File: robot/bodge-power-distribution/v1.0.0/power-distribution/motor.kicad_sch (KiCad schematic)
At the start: 6 parts, among them J4 MOTOR_{FL}, J5 MOTOR_{BL}, J6 MOTOR_{DRB}, J7 MOTOR_{AUX}, J8 MOTOR_{FR}, J9 MOTOR_{BR}

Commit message: Alpha (0.0.0)
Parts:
- added C30, C31: 10uF 63V, Capacitor_SMD:C_1210_3225Metric, symbol Device:C_Small
- added J12: MOTOR_{DRB}, AT-Connectors:1x02_P3mm_3x5mm_Plug_SMD, symbol Connector_Generic:Conn_01x02
- added J13: MOTOR_{AUX}, AT-Connectors:1x02_P3mm_3x5mm_Plug_SMD, symbol Connector_Generic:Conn_01x02
- added J16, J18: MOTOR_{FR}, AT-Connectors:1x02_P3mm_3x5mm_Plug_SMD, symbol Connector_Generic:Conn_01x02
- added J17: MOTOR_{BR}, AT-Connectors:1x02_P3mm_3x5mm_Plug_SMD, symbol Connector_Generic:Conn_01x02
- added J19: SERVO, Connector_PinSocket_2.54mm:PinSocket_1x03_P2.54mm_Vertical, symbol Connector_Generic:Conn_01x03
- added J8: MOTOR_{FL}, AT-Connectors:1x02_P3mm_3x5mm_Plug_SMD, symbol Connector_Generic:Conn_01x02
- added J9: MOTOR_{BL}, AT-Connectors:1x02_P3mm_3x5mm_Plug_SMD, symbol Connector_Generic:Conn_01x02
- added U7: DRV8220, Package_TO_SOT_SMD:SOT-563, symbol AT-PowerIC:DRV8220
- renumbered J6 to J10, J7 to J11, J8 to J14, J9 to J15, J4 to J6, J5 to J7
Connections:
- new net: J18.2 (Pin_2), U7.4 (OUT2)
- new net: J18.1 (Pin_1), U7.6 (OUT1)
- new net +12V: C30.1, U7.5 (VM)
- new net +5V: C31.1, J19.2 (Pin_2)
- new net +V_{BATT(PROTECTED)}: J12.1 (Pin_1), J13.1 (Pin_1), J16.1 (Pin_1), J17.1 (Pin_1), J8.1 (Pin_1), J9.1 (Pin_1)
- new net GND: C30.2, C31.2, J12.2 (Pin_2), J13.2 (Pin_2), J16.2 (Pin_2), J17.2 (Pin_2), J19.3 (Pin_3), J8.2 (Pin_2), J9.2 (Pin_2), U7.3 (GND)
- new net MOTOR_{BRUSHED}.IN1: U7.1 (IN1)
- new net MOTOR_{BRUSHED}.IN2: U7.2 (IN2)
- new net MOTOR_{SERVO}.SIG: J19.1 (Pin_1)

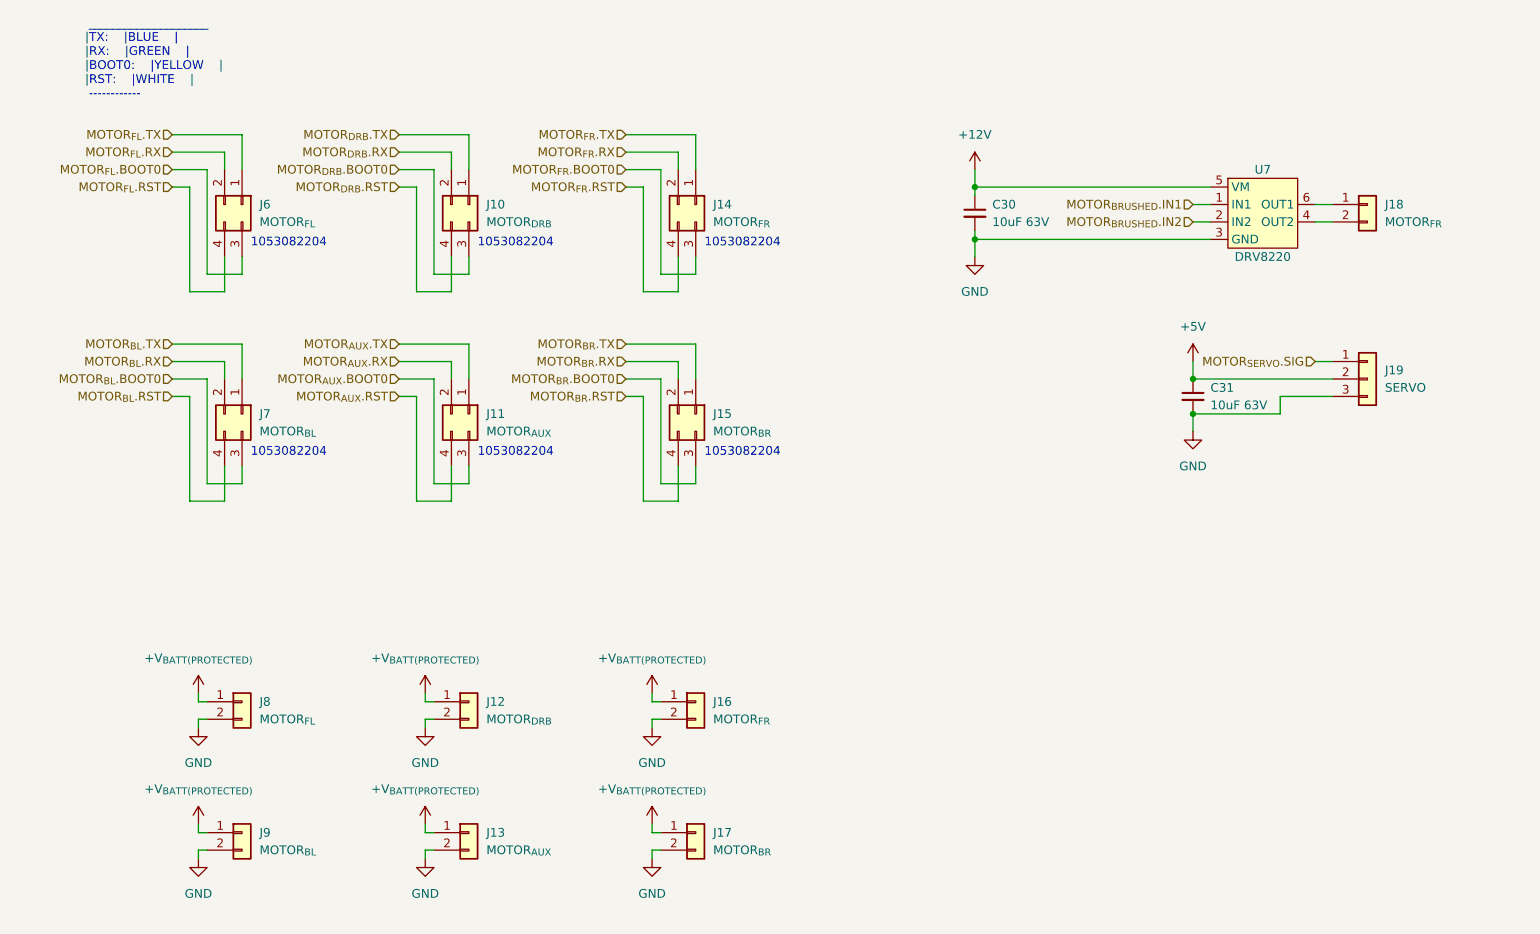
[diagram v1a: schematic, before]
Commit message: Schematic aesthetics & formatting
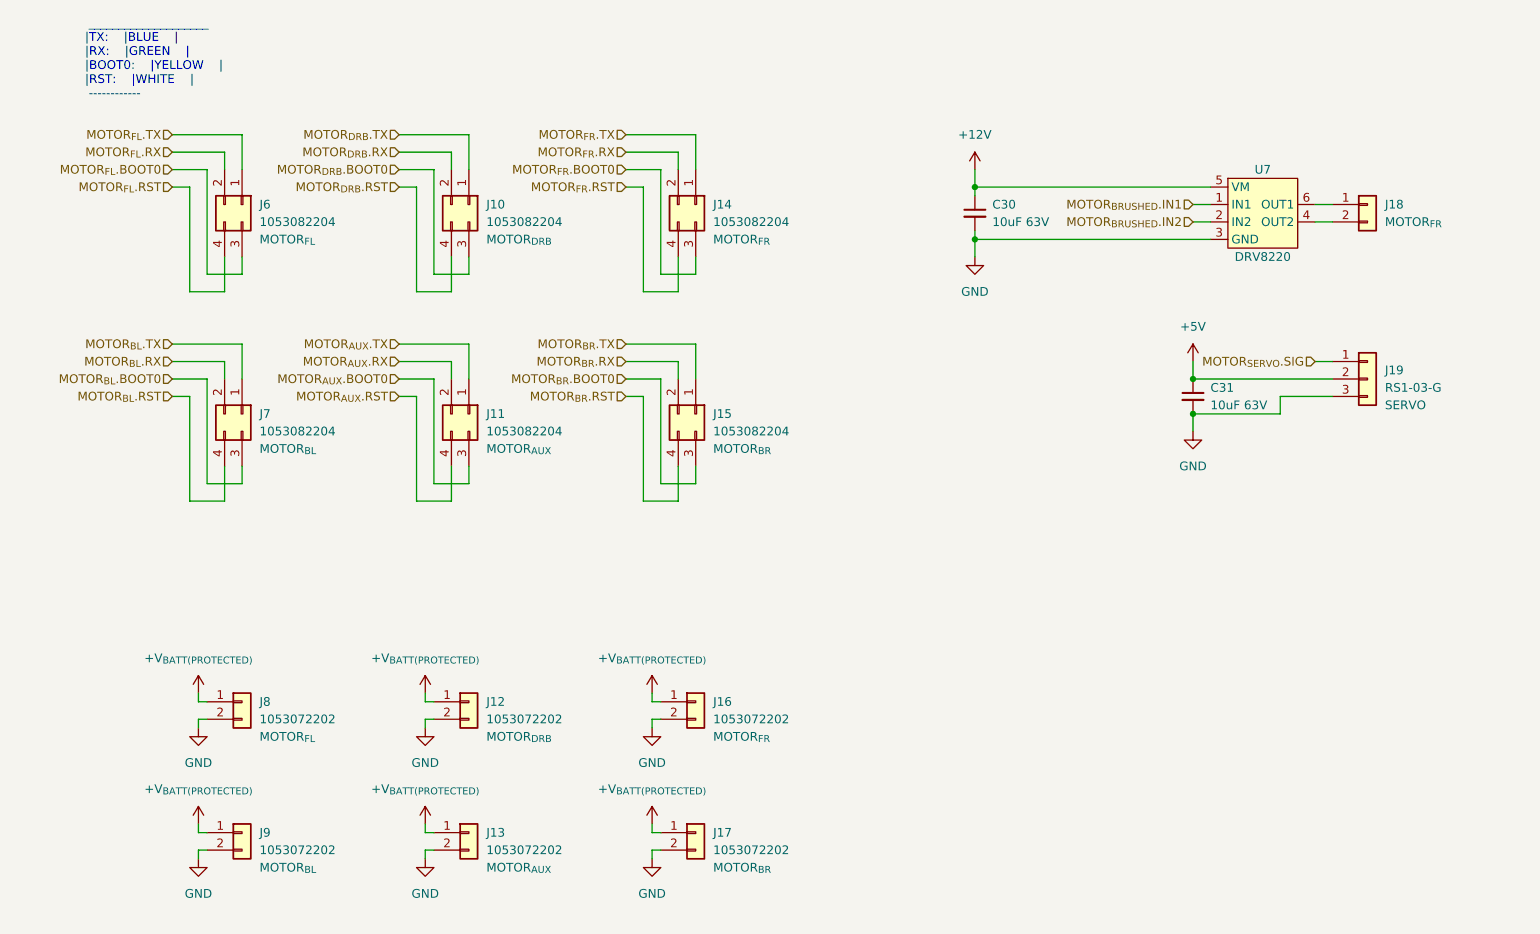
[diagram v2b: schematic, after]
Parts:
- J10: value MOTOR_{DRB} -> 1053082204; Value2 (none) -> MOTOR_{DRB}
- J11: value MOTOR_{AUX} -> 1053082204; Value2 (none) -> MOTOR_{AUX}
- J12: value MOTOR_{DRB} -> 1053072202; Value2 (none) -> MOTOR_{DRB}
- J13: value MOTOR_{AUX} -> 1053072202; Value2 (none) -> MOTOR_{AUX}
- J14: value MOTOR_{FR} -> 1053082204; Value2 (none) -> MOTOR_{FR}
- J15: value MOTOR_{BR} -> 1053082204; Value2 (none) -> MOTOR_{BR}
- J16: value MOTOR_{FR} -> 1053072202; Value2 (none) -> MOTOR_{FR}
- J17: value MOTOR_{BR} -> 1053072202; Value2 (none) -> MOTOR_{BR}
- J18: now left out of the parts list
- J19: value SERVO -> RS1-03-G; Value2 (none) -> SERVO
- J6: value MOTOR_{FL} -> 1053082204; Value2 (none) -> MOTOR_{FL}
- J7: value MOTOR_{BL} -> 1053082204; Value2 (none) -> MOTOR_{BL}
- J8: value MOTOR_{FL} -> 1053072202; Value2 (none) -> MOTOR_{FL}
- J9: value MOTOR_{BL} -> 1053072202; Value2 (none) -> MOTOR_{BL}
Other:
- note removed: "1053082204"

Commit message: Minor updates
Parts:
- J18: value MOTOR_{FR} -> MOTOR_{BRUSHED}
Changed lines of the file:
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@@
       (effects (font (size 1.27 1.27)) (justify left))
     )
-    (property "Value" "MOTOR_{FR}" (id 1) (at 217.17 49.5299 0)
+    (property "Value" "MOTOR_{BRUSHED}" (id 1) (at 217.17 49.5299 0)
       (effects (font (size 1.27 1.27)) (justify left))
     )

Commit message: Post-review updates
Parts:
- J12, J13, J16, J17, J8, J9: footprint AT-Connectors:1x02_P3mm_3x5mm_Plug_SMD -> AT-Connectors:1x03_P3mm_ID0.8mm_OD2mm_Plug_TH; symbol Connector_Generic:Conn_01x02 -> Connector_Generic:Conn_01x03
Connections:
- net +5V: now also J12.2 (Pin_2), J13.2 (Pin_2), J16.2 (Pin_2), J17.2 (Pin_2), J8.2 (Pin_2), J9.2 (Pin_2)
- net GND: now also J12.3 (Pin_3), J13.3 (Pin_3), J16.3 (Pin_3), J17.3 (Pin_3), J8.3 (Pin_3), J9.3 (Pin_3); no longer J12.2 (Pin_2), J13.2 (Pin_2), J16.2 (Pin_2), J17.2 (Pin_2), J8.2 (Pin_2), J9.2 (Pin_2)

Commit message: Prepare files for production
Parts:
- J10, J11, J12, J13, J14, J15, J16, J17, J6, J7, J8, J9: now left out of the parts list
- renumbered C30 to C34, C31 to C35
